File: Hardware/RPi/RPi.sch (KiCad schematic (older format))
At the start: 94 parts, among them P1 USB_B, P10 Solder_Pad, P11 Solder_Pad, P12 Solder_Pad, P13 Solder_Pad, P14 Solder_Pad, P15 Solder_Pad, P16 Solder_Pad, P17 Solder_Pad, P18 Solder_Pad, P19 Solder_Pad, P2 CONN_01X06, P20 Solder_Pad, P21 Solder_Pad, P7 Solder_Pad, P8 Solder_Pad, P9 Solder_Pad, U1 MPU_9150, U10 WS2812B, U11 WS2812B, U12 WS2812B, U13 Teensy_LC, U14 WS2812B, U15 WS2812B, U16 WS2812B, U17 WS2812B, U18 WS2812B, U19 WS2812B, U2 RPi_Interface, U20 SolderpadPowerOut, U21 SolderpadPowerOut, U22 USB_Solder_Pad, U23 USB_Solder_Pad, U24 USB_Solder_Pad, U25 USB_Solder_Pad, U3 FE1.1s, U4 AP1117E25, U5 Dual_buffer_NC7WZ16, U6 ESP-12E, U7 WS2812B, U8 WS2812B, U9 WS2812B, Y1 Crystal 12MHz

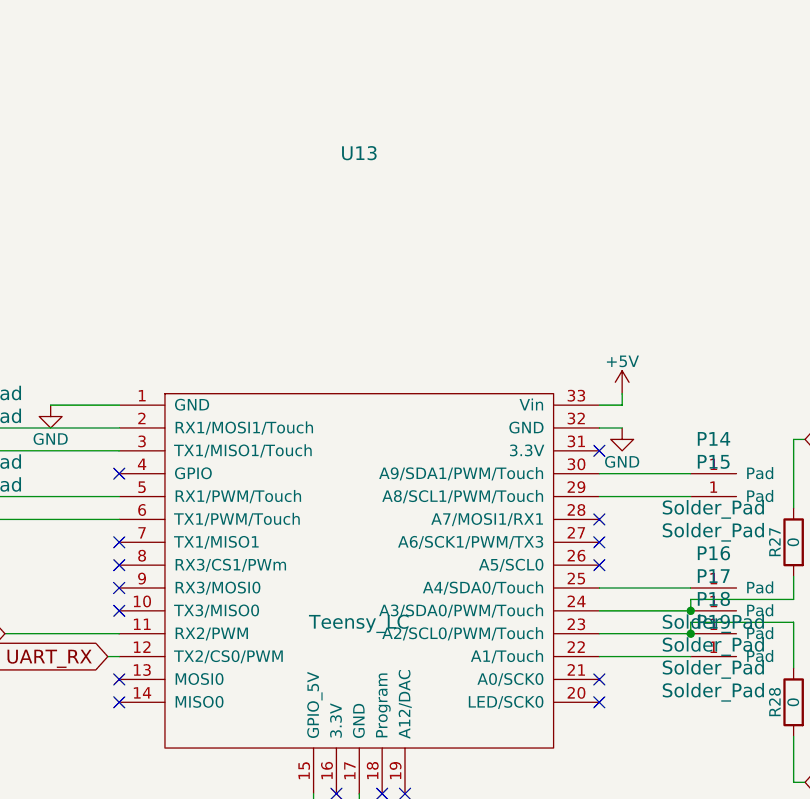
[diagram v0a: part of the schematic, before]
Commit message: Trying to fix the teensyLC footprint
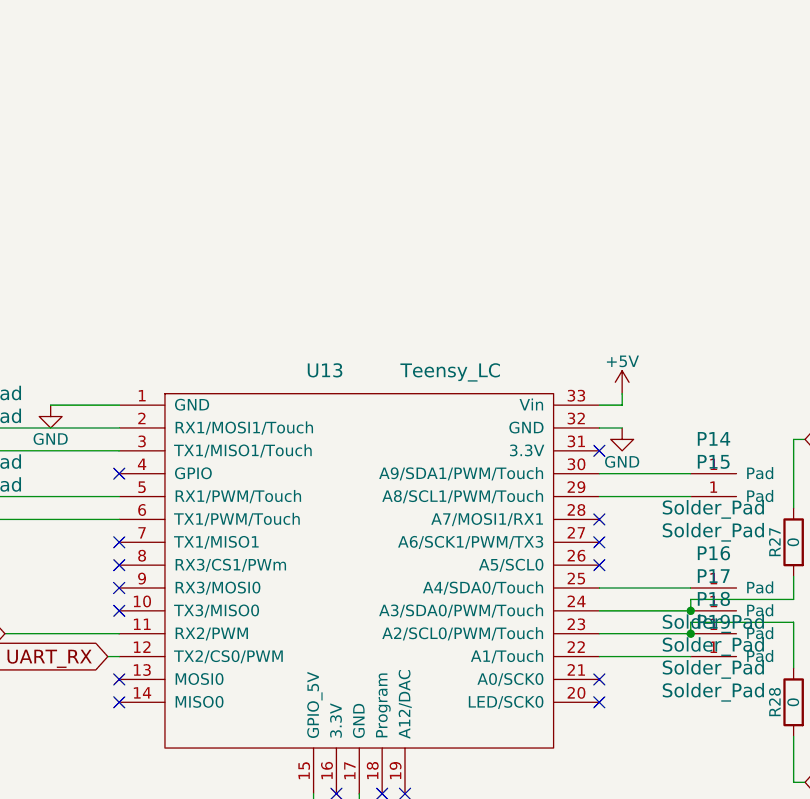
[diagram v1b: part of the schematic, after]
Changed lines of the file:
@@
 Thanks to: https://github.com/al177/wifi_pants
-$Comp
-L Teensy_LC U13
-U 1 1 56C74A7F
-P 13150 1300
-F 0 "U13" H 13150 2600 60  0000 C CNN
-F 1 "Teensy_LC" H 13150 550 60  0000 C CNN
-F 2 "TimeArc:TeensyLC" H 13150 1300 60  0001 C CNN
-F 3 "" H 13150 1300 60  0000 C CNN
-	1    13150 1300
-	1    0    0    -1
-$EndComp
 $Comp
 L +5V #PWR041
@@
 Wire Wire Line
 	5700 8200 5500 8200
+$Comp
+L Teensy_LC U13
+U 1 1 5705A33E
+P 13150 1300
+F 0 "U13" H 13000 1650 60  0000 C CNN
+F 1 "Teensy_LC" H 13550 1650 60  0000 C CNN
+F 2 "TimeArc:TeensyLC" H 13100 300 60  0001 C CNN
+F 3 "" H 13100 300 60  0000 C CNN
+	1    13150 1300
+	1    0    0    -1
+$EndComp
 $EndSCHEMATC

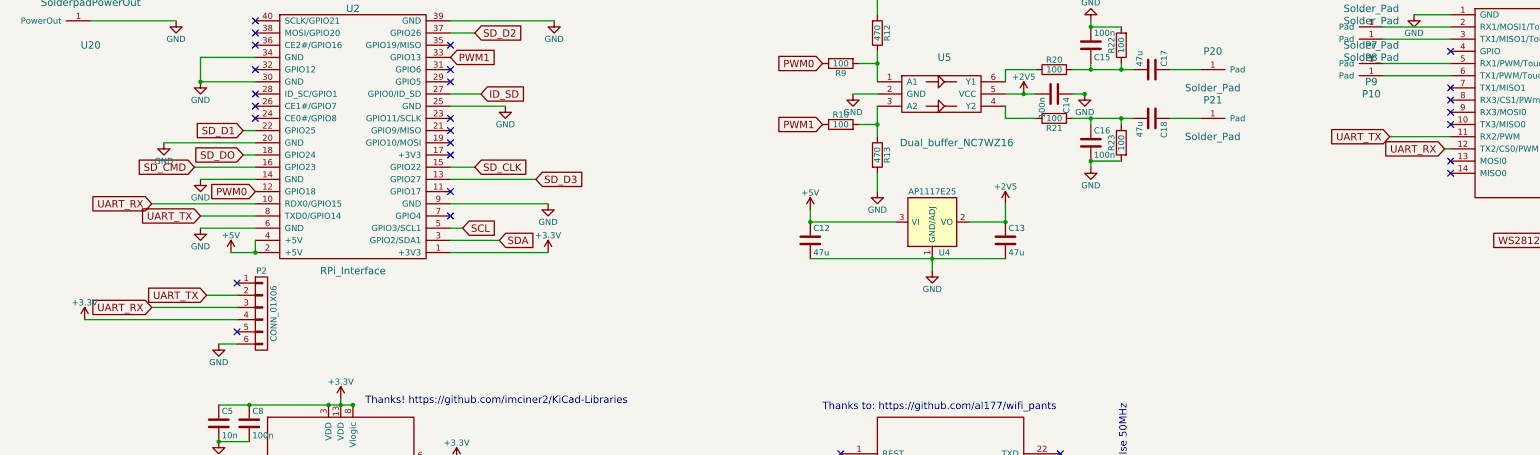
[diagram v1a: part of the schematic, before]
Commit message: Removed FTDI header, removed all unused footprints
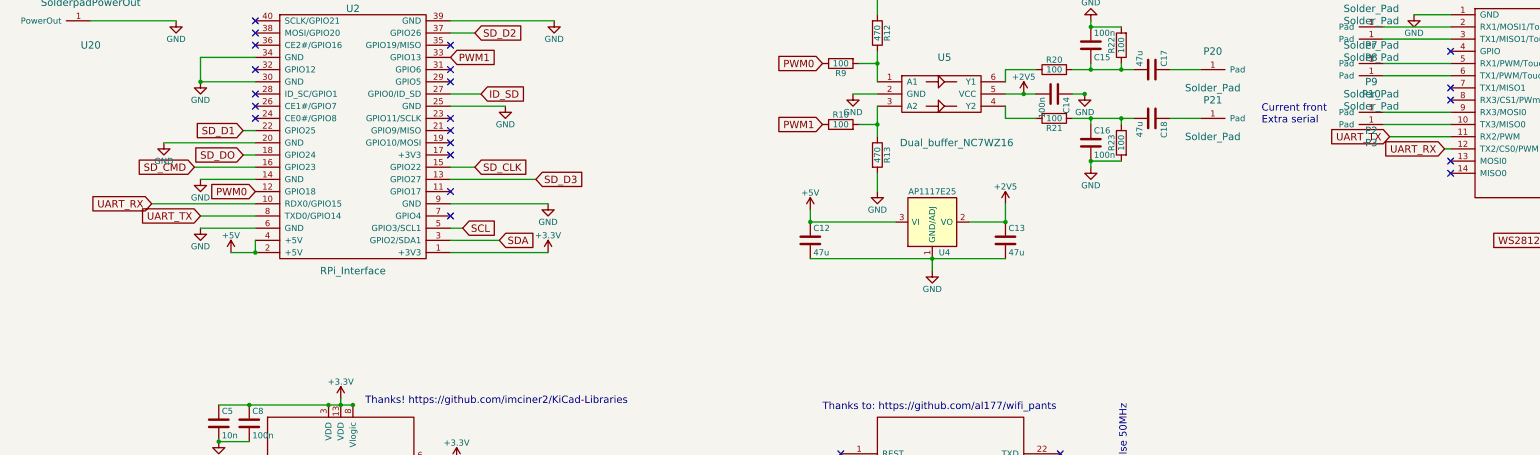
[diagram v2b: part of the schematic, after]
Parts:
- removed P2: CONN_01X06, TimeArc:1x06 pinheader smd, symbol CONN_01X06
- added P2, P3: Solder_Pad, Measurement_Points:Measurement_Point_Square-SMD-Pad_Big, symbol Solder_Pad
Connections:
- net at U13.10 (TX3/MISO0): now also P3.1 (Pad)
- net at U13.9 (RX3/MOSI0): now also P2.1 (Pad)
- no-connect marks 53 -> 49
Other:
- note added: "Current front\nExtra serial"
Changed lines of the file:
@@
 NoConn ~ 12100 1700
 NoConn ~ 12100 1800
-NoConn ~ 12100 1900
-NoConn ~ 12100 2000
 NoConn ~ 12100 2300
 NoConn ~ 12100 2400
@@
 Text GLabel 11600 2100 0    60   Input ~ 0
 UART_TX
-$Comp
-L CONN_01X06 P2
-U 1 1 56CBC91E
-P 2350 3550
-F 0 "P2" H 2350 3900 50  0000 C CNN
-F 1 "CONN_01X06" V 2450 3550 50  0000 C CNN
-F 2 "TimeArc:1x06 pinheader smd" H 2350 3550 50  0001 C CNN
-F 3 "" H 2350 3550 50  0000 C CNN
-	1    2350 3550
-	1    0    0    -1
-$EndComp
-Text GLabel 1900 3400 0    60   Input ~ 0
-UART_TX
-Text GLabel 1450 3500 0    60   Input ~ 0
-UART_RX
-$Comp
-L +3.3V #PWR076
-U 1 1 56CC7CD4
-P 900 3600
-F 0 "#PWR076" H 900 3450 50  0001 C CNN
-F 1 "+3.3V" H 900 3740 50  0000 C CNN
-F 2 "" H 900 3600 50  0000 C CNN
-F 3 "" H 900 3600 50  0000 C CNN
-	1    900  3600
-	1    0    0    -1
-$EndComp
-$Comp
-L GND #PWR077
-U 1 1 56CC7FB4
-P 2000 3800
-F 0 "#PWR077" H 2000 3550 50  0001 C CNN
-F 1 "GND" H 2000 3650 50  0000 C CNN
-F 2 "" H 2000 3800 50  0000 C CNN
-F 3 "" H 2000 3800 50  0000 C CNN
-	1    2000 3800
-	1    0    0    -1
-$EndComp
 Wire Wire Line
 	7250 2000 7400 2000
@@
 Wire Wire Line
 	1150 9200 950  9200
-Wire Wire Line
-	1450 3500 2150 3500
-Wire Wire Line
-	2150 3400 1900 3400
-Wire Wire Line
-	900  3600 2150 3600
-Wire Wire Line
-	2150 3800 2000 3800
 NoConn ~ 7100 4700
 NoConn ~ 7100 4900
@@
 Wire Wire Line
 	14850 7200 14750 7200
-NoConn ~ 2150 3300
-NoConn ~ 2150 3700
 $Comp
 L RPi_Interface U2
@@
 $EndComp
 $Comp
-L +5V #PWR078
+L +5V #PWR076
 U 1 1 57054E73
 P 1650 750
-F 0 "#PWR078" H 1650 600 50  0001 C CNN
+F 0 "#PWR076" H 1650 600 50  0001 C CNN
 F 1 "+5V" H 1650 890 50  0000 C CNN
 F 2 "" H 1650 750 50  0000 C CNN
@@
 $EndComp
 $Comp
-L GND #PWR079
+L GND #PWR077
 U 1 1 570558BC
 P 1650 1150
-F 0 "#PWR079" H 1650 900 50  0001 C CNN
+F 0 "#PWR077" H 1650 900 50  0001 C CNN
 F 1 "GND" H 1650 1000 50  0000 C CNN
 F 2 "" H 1650 1150 50  0000 C CNN
@@
 	1    0    0    -1
 $EndComp
+$Comp
+L Solder_Pad P3
+U 1 1 570D81A8
+P 11450 2000
+F 0 "P3" H 11450 2150 60  0000 C CNN
+F 1 "Solder_Pad" H 11450 1850 60  0000 C CNN
+F 2 "Measurement_Points:Measurement_Point_Square-SMD-Pad_Big" H 11450 2000 60  0001 C CNN
+F 3 "" H 11450 2000 60  0000 C CNN
+	1    11450 2000
+	-1   0    0    1
+$EndComp
+$Comp
+L Solder_Pad P2
+U 1 1 570D833E
+P 11450 1900
+F 0 "P2" H 11450 2050 60  0000 C CNN
+F 1 "Solder_Pad" H 11450 1750 60  0000 C CNN
+F 2 "Measurement_Points:Measurement_Point_Square-SMD-Pad_Big" H 11450 1900 60  0001 C CNN
+F 3 "" H 11450 1900 60  0000 C CNN
+	1    11450 1900
+	-1   0    0    1
+$EndComp
+Wire Wire Line
+	12100 2000 11550 2000
+Wire Wire Line
+	12100 1900 11550 1900
+Text Notes 10550 2000 0    60   ~ 0
+Current front\nExtra serial
 $EndSCHEMATC

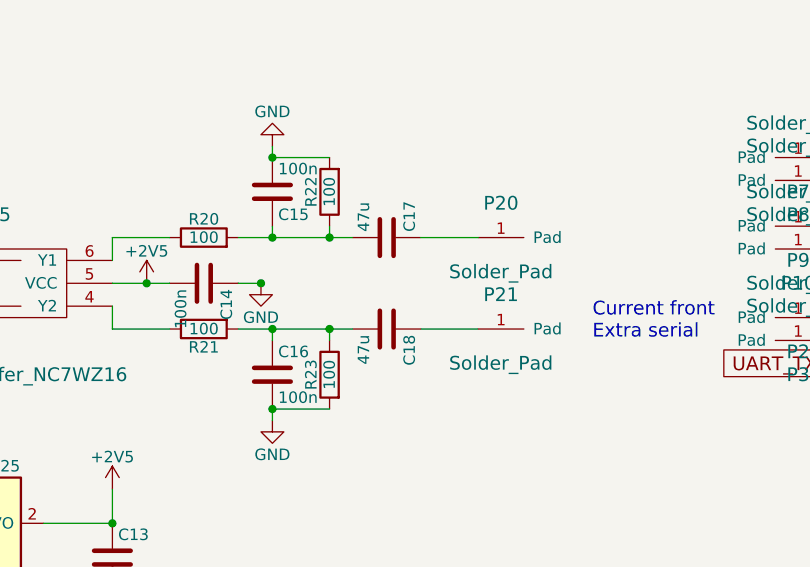
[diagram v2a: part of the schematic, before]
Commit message: Placing stuff on the board
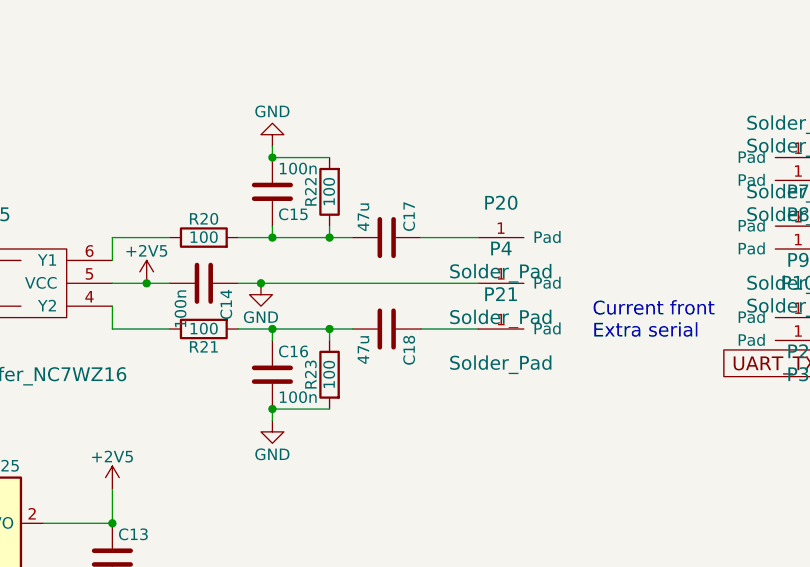
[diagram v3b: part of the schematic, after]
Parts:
- added P4: Solder_Pad, Measurement_Points:Measurement_Point_Square-SMD-Pad_Big, symbol Solder_Pad
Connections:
- net GND: now also P4.1 (Pad)
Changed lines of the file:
@@
 Connection ~ 8600 1750
 Wire Wire Line
-	9100 1750 9000 1750
+	9000 1750 10050 1750
 Wire Wire Line
 	7250 1500 7400 1500
@@
 $EndComp
 $Comp
-L Solder_Pad P3
-U 1 1 570D81A8
-P 11450 2000
-F 0 "P3" H 11450 2150 60  0000 C CNN
-F 1 "Solder_Pad" H 11450 1850 60  0000 C CNN
-F 2 "Measurement_Points:Measurement_Point_Square-SMD-Pad_Big" H 11450 2000 60  0001 C CNN
-F 3 "" H 11450 2000 60  0000 C CNN
-	1    11450 2000
-	-1   0    0    1
-$EndComp
-$Comp
 L Solder_Pad P2
 U 1 1 570D833E
@@
 Text Notes 10550 2000 0    60   ~ 0
 Current front\nExtra serial
+$Comp
+L Solder_Pad P4
+U 1 1 570E35ED
+P 10150 1750
+F 0 "P4" H 10150 1900 60  0000 C CNN
+F 1 "Solder_Pad" H 10150 1600 60  0000 C CNN
+F 2 "Measurement_Points:Measurement_Point_Square-SMD-Pad_Big" H 10150 1750 60  0001 C CNN
+F 3 "" H 10150 1750 60  0000 C CNN
+	1    10150 1750
+	1    0    0    -1
+$EndComp
+$Comp
+L Solder_Pad P3
+U 1 1 570EFEC2
+P 11450 2000
+F 0 "P3" H 11450 2150 60  0000 C CNN
+F 1 "Solder_Pad" H 11450 1850 60  0000 C CNN
+F 2 "Measurement_Points:Measurement_Point_Square-SMD-Pad_Big" H 11450 2000 60  0001 C CNN
+F 3 "" H 11450 2000 60  0000 C CNN
+	1    11450 2000
+	-1   0    0    1
+$EndComp
 $EndSCHEMATC

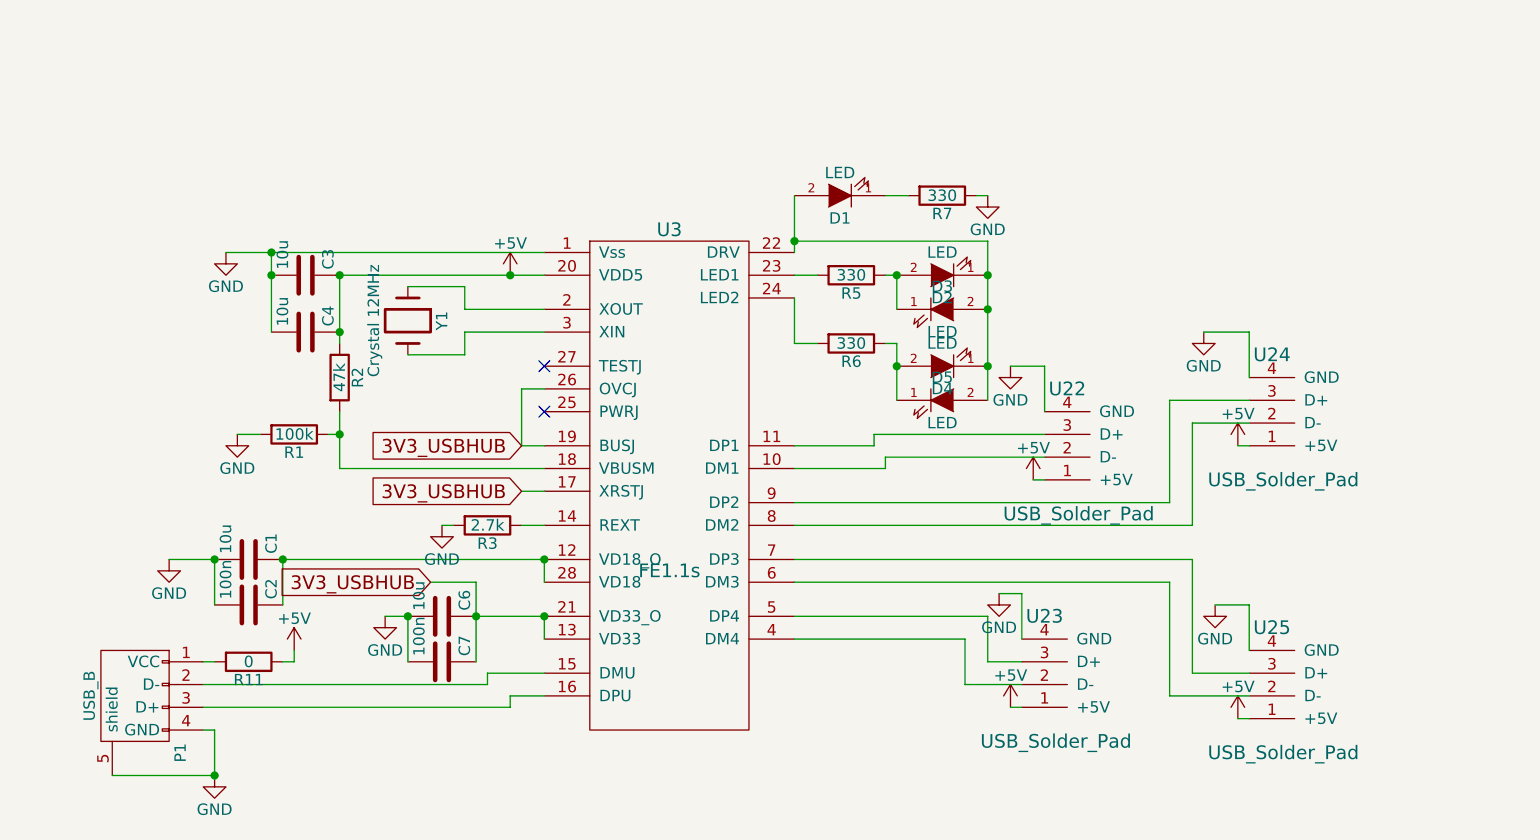
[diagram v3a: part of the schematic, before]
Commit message: Removed USB hub, ordered pcb
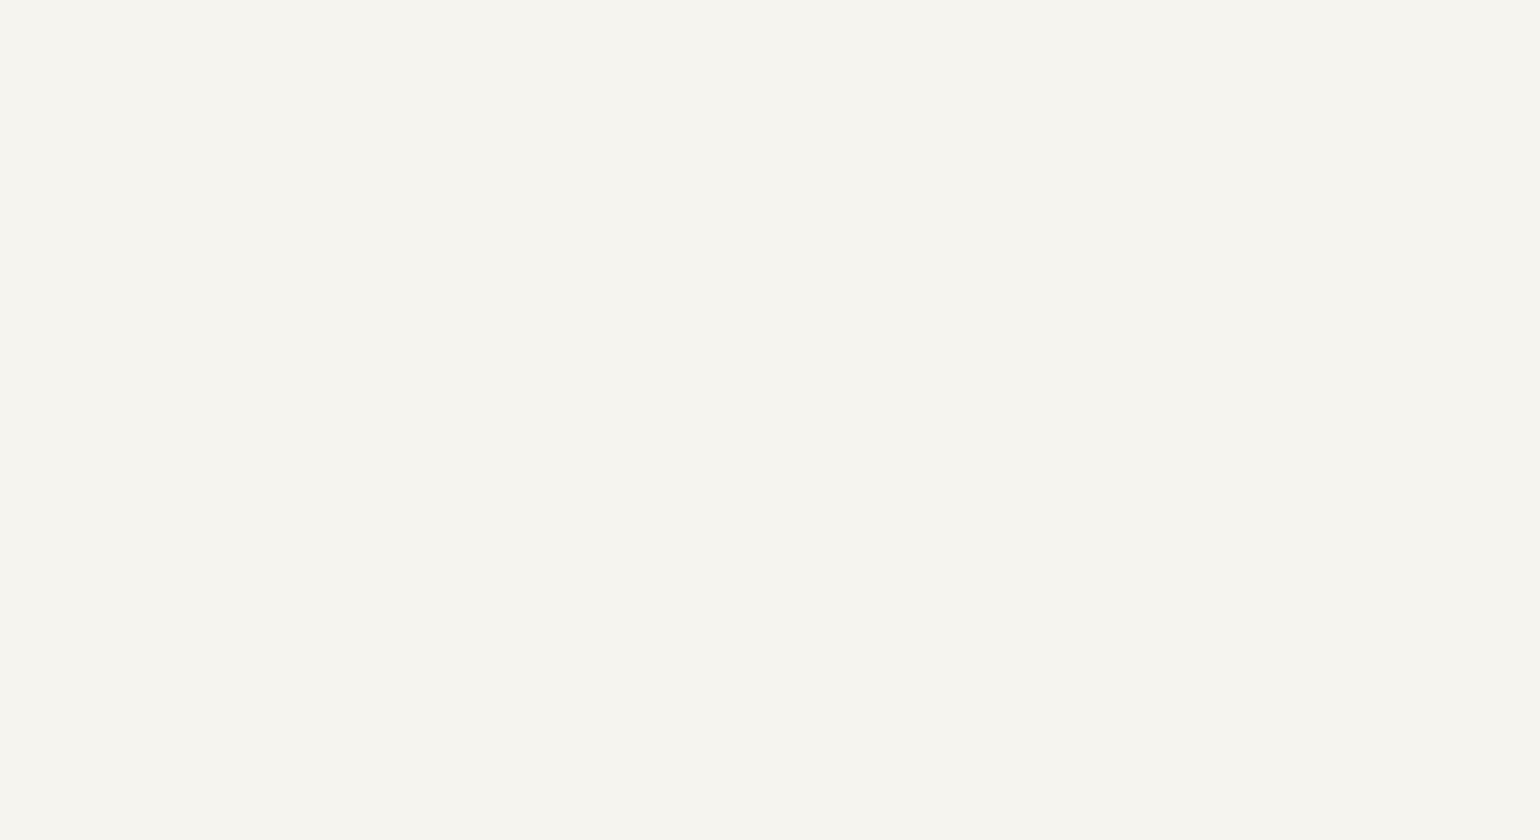
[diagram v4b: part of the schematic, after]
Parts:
- removed C1, C3, C4, C6: 10u, Capacitors_SMD:C_0603, symbol C
- removed C2, C7: 100n, Capacitors_SMD:C_0603, symbol C
- removed D1, D2, D3, D4, D5: LED, LEDs:LED_0603, symbol LED
- removed P1: USB_B, Connect:USB_Mini-B, symbol USB_B
- removed R1: 100k, Resistors_SMD:R_0603, symbol R
- removed R11: 0, Resistors_SMD:R_0603, symbol R
- removed R2: 47k, Resistors_SMD:R_0603, symbol R
- removed R3: 2.7k, Resistors_SMD:R_0603, symbol R
- removed R5, R6, R7: 330, Resistors_SMD:R_0603, symbol R
- removed U22, U23, U24, U25: USB_Solder_Pad, TimeArc:USB_A_SMD_Pads, symbol USB_Solder_Pad
- removed U3: FE1.1s, Housings_SSOP:SSOP-28_5.3x10.2mm_Pitch0.65mm, symbol FE1.1s
- removed Y1: Crystal 12MHz, TimeArc:Crystal_12MHz, symbol Crystal
- U5: footprint TO_SOT_Packages_SMD:SC-70 -> TO_SOT_Packages_SMD:SC-70-6_Handsoldering
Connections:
- no-connect marks 49 -> 47
